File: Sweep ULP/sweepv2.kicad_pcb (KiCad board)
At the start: 2 copper layers, 216.9 x 86.9 mm, 47 parts, among them SW10 SW_Push, SW10_r1 SW_Push, SW11 SW_Push, SW11_r1 SW_Push, SW12 SW_Push, SW12_r1 SW_Push, SW13_r1 SW_Push, SW14 SW_Push, SW14_r1 SW_Push, SW15 SW_Push, SW15_r1 SW_Push, SW16 SW_Push, SW16_r1 SW_Push, SW17 SW_Push, SW17_r1 SW_Push, SW18 SW_Push, SW18_r1 SW_Push, SW2 SW_Push, SW20 SW_Push, SW21 SW_Push, SW2_r1 SW_Push, SW3 SW_Push, SW3_r1 SW_Push, SW4 SW_Push, SW4_r1 SW_Push, SW5 SW_Push, SW5_r1 SW_Push, SW6 SW_Push, SW6_r1 SW_Push, SW7_r1 SW_Push, SW8 SW_Push, SW8_r1 SW_Push, SW9 SW_Push, SW9_r1 SW_Push, U1 ProMicro-kbd, U2 ProMicro-kbd

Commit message: hexed ground and added crab
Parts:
- SW_POWER1, SW_POWERR1: moved to F.Cu
- turned SW_POWER1 to 0 degrees
- turned SW_POWERR1 to 0 degrees
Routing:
- net gnd: track 5.91 -> 452.9 mm, vias 2 -> 1
- net raw: track 29.7 -> 20.3 mm
- net Switch17: track 50.9 -> 49.9 mm
- net BT+: track 9.45 -> 8.65 mm
- net Switch15: track 46.3 -> 45.6 mm
- net Switch8: track 85.1 -> 85.7 mm
- net Switch9: track 63.2 -> 63.7 mm
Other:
- board text added: "Swulp by Purox. Swulp is based on Sweep, Sweep is based on the Ferris."
- board text removed: "Sweep is based on the Ferris."
- board text removed: "Sweep v 2.2"

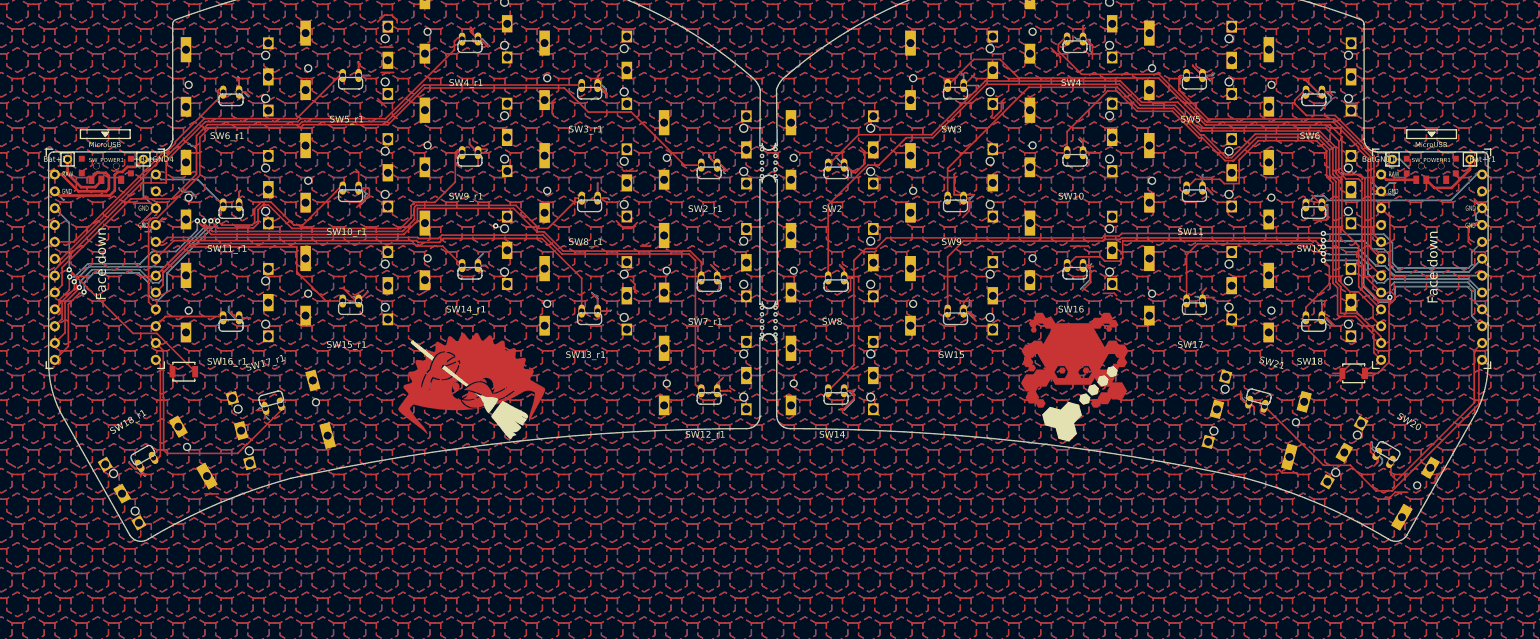
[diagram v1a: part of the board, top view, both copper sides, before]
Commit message: moved batteries and switches around
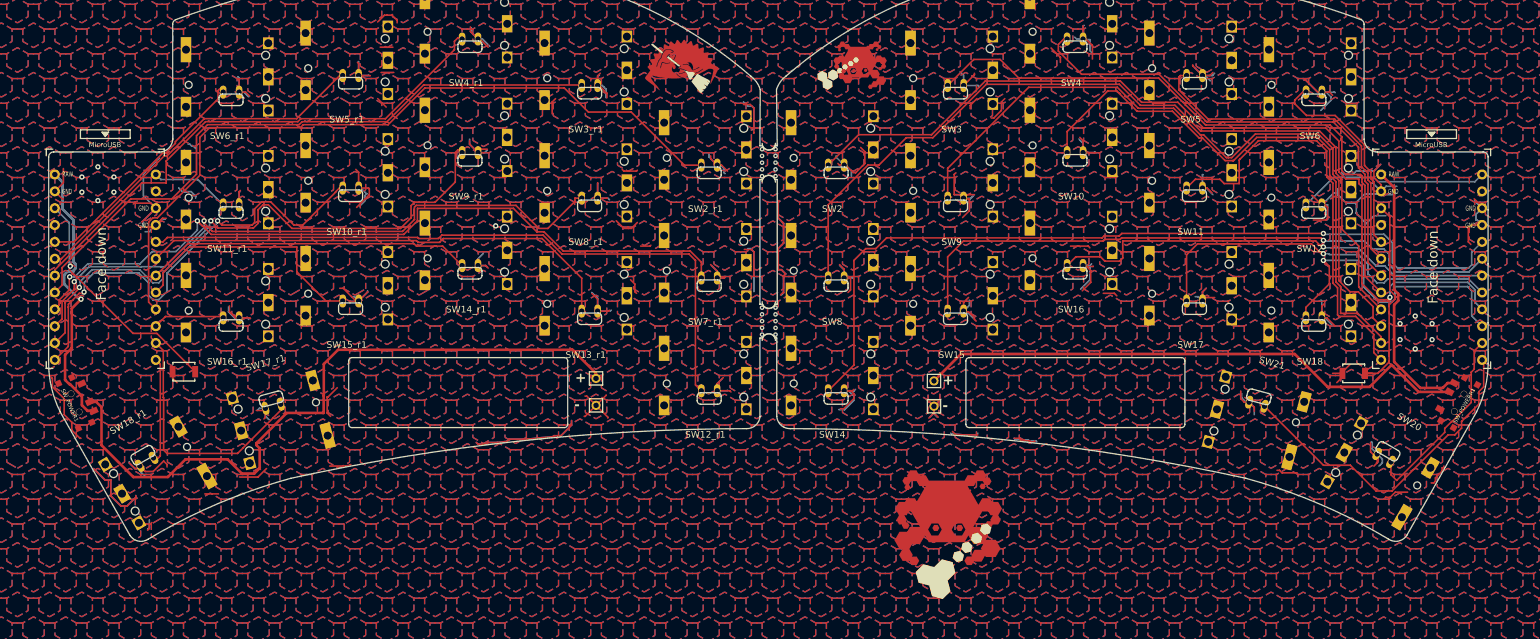
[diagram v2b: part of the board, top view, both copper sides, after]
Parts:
- G***: footprint Kailh:ferris_broom -> ulp-footprints:ferris_broom0.5
- moved Bat+r1 87.4 mm to (155.2, 84.2)
- moved Bat+1 86.2 mm to (104.3, 83.8)
- moved BatGND1 78.5 mm to (155.2, 88.0)
- moved BatGND4 77.6 mm to (104.3, 87.9)
- moved G*** 58.2 mm to (116.5, 37.0)
- moved SW_POWER1 36.0 mm to (25.8, 87.5), turned to 114 degrees
- moved SW_POWERR1 35.9 mm to (234.3, 87.5), turned to -119 degrees
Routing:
- net gnd: track 452.9 -> 636.5 mm, vias 1 -> 13
- net BT+: track 8.65 -> 103.5 mm
- net BT+_r: track 9.78 -> 84.5 mm
- net raw: track 20.3 -> 83.3 mm, vias 0 -> 1
- net Switch17: track 49.9 -> 50.7 mm
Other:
- outline, holes or cut-outs redrawn
- board text added: "+"
- board text added: "-"
